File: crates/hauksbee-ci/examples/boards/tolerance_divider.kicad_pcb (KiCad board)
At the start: 2 parts

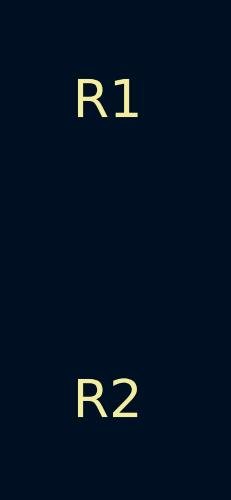
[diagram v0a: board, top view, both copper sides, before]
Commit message: Static-gate fallout: physical fixtures, true findings kept, two false alarms fixed by invariant
The CI run fails on every finding that gates `hauksbee check`. The fixtures
and tests that broke under that rule now follow it, and none of them hide it.

- Synthetic fixtures are physically valid: pads are spaced and copper is
 routed where a board must check clean. The d2pak and adj-regulator boards
 use 1210 resistors, and the comparator board has its J1 supply.
- Board-as-Code fixtures can't carry copper. Each one has a visible
 [[waive]] for unrouted_pad with a reason, and its test asserts that the
 waived row is still listed.
- The tolerance_divider example board routes VOUT, so blinky-permissive and
 the divider examples no longer fail on "not routed".
- True findings keep their rows, and the expectations now say so:
 - Tarski unlimited_base_drive: the BCM847BS base is driven from the
 LVC1G3157 B2/A channel through rON only.
 - Tarski cap_no_dc_path: the 1N4148 reverse leakage is bounded only from
 above.
 The repaired flagship and neuron examples are RED only on those rows, and
 the docs are updated to match.
- Strap lint (false alarm, Olimex rev L): a carded voltage detector that
 holds the oscillator enable low counts as following the MCU reset when its
 sense node is fed only by:
 - resistors from the reset net
 - capacitors to ground
 - discharge-only diode anodes, read from the diode card
 This is decided from topology and cards, not from net names. It adds a
 legal control and a faulty control.
- power_pin_wiring (false alarm, CP2104 VIO tied to VDD): the new
 optional_supplies.regulated_from field says the pin is an on-chip
 regulator's output. When that regulator's input is fed, the pin feeds the
 part's other supplies.
 - CP2102 and CP2104 gain this field.
 - MAX17760 VCC is an optional (LDO output) supply.
 - The datasheet basis is cited in each card.
- The CI static gate reports waived rows separately, and a measurement-only
 run beside a waived row st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
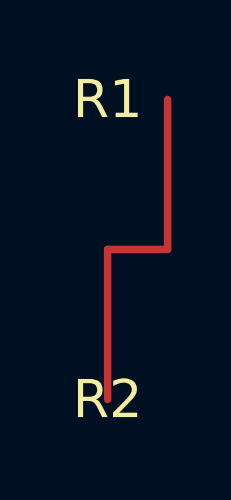
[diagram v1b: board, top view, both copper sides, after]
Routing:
- net VOUT: track 0.00 -> 12.0 mm
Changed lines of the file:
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@@
     (pad 2 thru_hole circle (at 2 0) (net 1 "GND"))
   )
+  (segment (start 102 100) (end 102 105) (width 0.25) (layer F.Cu) (net 3))
+  (segment (start 102 105) (end 100 105) (width 0.25) (layer F.Cu) (net 3))
+  (segment (start 100 105) (end 100 110) (width 0.25) (layer F.Cu) (net 3))
 )
